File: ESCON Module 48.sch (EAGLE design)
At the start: 76 parts, among them U1 ESDA14V2SC6, U2 ESDA14V2SC6, U3 ESDA14V2SC6, X1 TERMINAL-BLOCK-3.5MM-2-PIN-LO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, X11 JST-XH-02-PIN-LONG-PAD, X12 JST-XH-03-PIN-LONG-PAD, X13 JST-XH-04-PIN-LONG-PAD, X14 JST-XH-03-PIN-LONG-PAD, X15 JST-XH-05-PIN-LONG-PAD, X17 JST-XH-02-PIN-LONG-PAD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

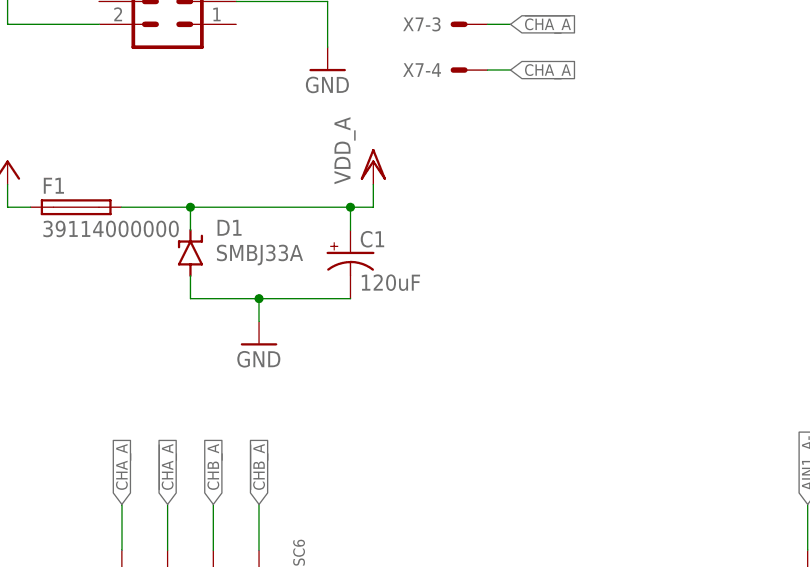
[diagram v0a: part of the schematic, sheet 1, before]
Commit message: Bigger capacitors
Added support for 3300uF capacitors
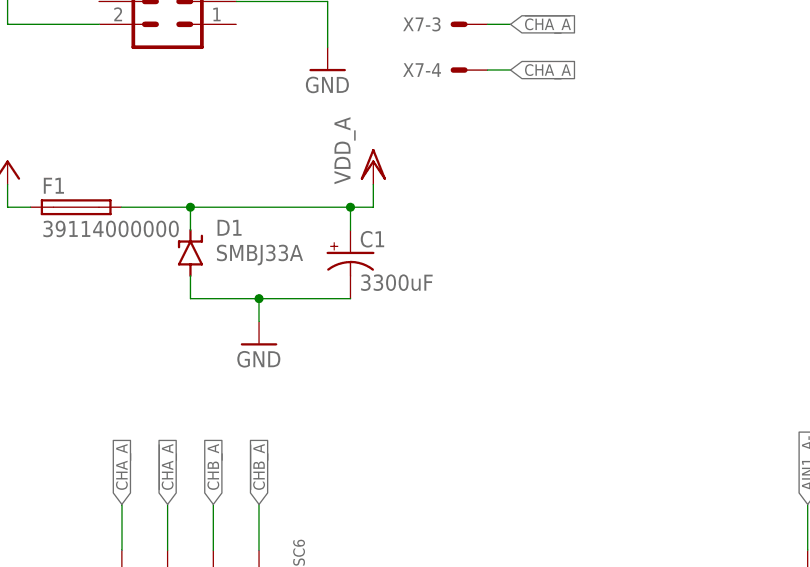
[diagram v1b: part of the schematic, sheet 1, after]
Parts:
- C1, C15, C8: value 120uF -> 3300uF; device rcl:CPOL-USE7.5-16 -> rcl:CPOL-USE7.5-18
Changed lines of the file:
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@@
 <parts>
 <part name="FRAME1" library="frames" library_urn="urn:adsk.eagle:library:229" deviceset="LETTER_L" device=""/>
-<part name="C1" library="rcl" library_urn="urn:adsk.eagle:library:334" deviceset="CPOL-US" device="E7.5-16" package3d_urn="urn:adsk.eagle:package:23382/2" value="120uF"/>
+<part name="C1" library="rcl" library_urn="urn:adsk.eagle:library:334" deviceset="CPOL-US" device="E7.5-18" package3d_urn="urn:adsk.eagle:package:23379/1" value="3300uF"/>
 <part name="D1" library="diode" library_urn="urn:adsk.eagle:library:210" deviceset="SUPPRESSOR-" device="SMBJ" package3d_urn="urn:adsk.eagle:package:43442/2" value="SMBJ33A"/>
 <part name="F1" library="fuse" library_urn="urn:adsk.eagle:library:233" deviceset="TE5" device="" package3d_urn="urn:adsk.eagle:package:14069/1" value="39114000000"/>
@@
 <part name="X7" library="Rembrandt Electronics - JST XH Connectors v1-0" deviceset="JST-XH-04-PIN" device="-LONG-PAD"/>
 <part name="FRAME2" library="frames" library_urn="urn:adsk.eagle:library:229" deviceset="LETTER_L" device=""/>
-<part name="C8" library="rcl" library_urn="urn:adsk.eagle:library:334" deviceset="CPOL-US" device="E7.5-16" package3d_urn="urn:adsk.eagle:package:23382/2" value="120uF"/>
+<part name="C8" library="rcl" library_urn="urn:adsk.eagle:library:334" deviceset="CPOL-US" device="E7.5-18" package3d_urn="urn:adsk.eagle:package:23379/1" value="3300uF"/>
 <part name="D3" library="diode" library_urn="urn:adsk.eagle:library:210" deviceset="SUPPRESSOR-" device="SMBJ" package3d_urn="urn:adsk.eagle:package:43442/2" value="SMBJ33A"/>
 <part name="F2" library="fuse" library_urn="urn:adsk.eagle:library:233" deviceset="TE5" device="" package3d_urn="urn:adsk.eagle:package:14069/1" value="39114000000"/>
@@
 <part name="X13" library="Rembrandt Electronics - JST XH Connectors v1-0" deviceset="JST-XH-04-PIN" device="-LONG-PAD"/>
 <part name="FRAME3" library="frames" library_urn="urn:adsk.eagle:library:229" deviceset="LETTER_L" device=""/>
-<part name="C15" library="rcl" library_urn="urn:adsk.eagle:library:334" deviceset="CPOL-US" device="E7.5-16" package3d_urn="urn:adsk.eagle:package:23382/2" value="120uF"/>
+<part name="C15" library="rcl" library_urn="urn:adsk.eagle:library:334" deviceset="CPOL-US" device="E7.5-18" package3d_urn="urn:adsk.eagle:package:23379/1" value="3300uF"/>
 <part name="D5" library="diode" library_urn="urn:adsk.eagle:library:210" deviceset="SUPPRESSOR-" device="SMBJ" package3d_urn="urn:adsk.eagle:package:43442/2" value="SMBJ33A"/>
 <part name="F3" library="fuse" library_urn="urn:adsk.eagle:library:233" deviceset="TE5" device="" package3d_urn="urn:adsk.eagle:package:14069/1" value="39114000000"/>
